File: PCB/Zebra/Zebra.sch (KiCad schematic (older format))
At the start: 10 parts, among them J1 Conn_01x05, J2 Conn_01x04, SW1 SW_Push, SW2 SW_Push, SW3 SW_Push, SW4 SW_Push

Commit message: Switch to foostan's footprint library, MIT license
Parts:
- SW1, SW2, SW3, SW4: footprint keyswitches:Kailh_socket_MX_optional -> kbd:CherryMX_Hotswap
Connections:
- net at SW1.1: now also J1.1 (Pin_1), SW2.1, SW3.1, SW4.1; no longer D1.2 (A)
- net at D2.2 (A): now also SW2.2; no longer SW2.1
- net at D3.2 (A): now also SW3.2; no longer SW3.1
- net at D4.2 (A): now also SW4.2; no longer SW4.1
- new net: D1.2 (A), SW1.2
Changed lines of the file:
@@
 Comment4 ""
 $EndDescr
-$Comp
-L Switch:SW_Push SW1
-U 1 1 5FA76D91
-P 2650 2000
-F 0 "SW1" H 2650 2285 50  0000 C CNN
-F 1 "SW_Push" H 2650 2194 50  0000 C CNN
-F 2 "keyswitches:Kailh_socket_MX_optional" H 2650 2200 50  0001 C CNN
-F 3 "~" H 2650 2200 50  0001 C CNN
-	1    2650 2000
-	1    0    0    -1
-$EndComp
 Wire Wire Line
 	2450 2000 2350 2000
@@
 F 0 "SW2" H 2650 2685 50  0000 C CNN
 F 1 "SW_Push" H 2650 2594 50  0000 C CNN
-F 2 "keyswitches:Kailh_socket_MX_optional" H 2650 2600 50  0001 C CNN
+F 2 "kbd:CherryMX_Hotswap" H 2650 2600 50  0001 C CNN
 F 3 "~" H 2650 2600 50  0001 C CNN
 	1    2650 2400
-	1    0    0    -1
+	-1   0    0    -1
 $EndComp
 $Comp
@@
 F 0 "SW3" H 2650 2985 50  0000 C CNN
 F 1 "SW_Push" H 2650 2894 50  0000 C CNN
-F 2 "keyswitches:Kailh_socket_MX_optional" H 2650 2900 50  0001 C CNN
+F 2 "kbd:CherryMX_Hotswap" H 2650 2900 50  0001 C CNN
 F 3 "~" H 2650 2900 50  0001 C CNN
 	1    2650 2700
-	1    0    0    -1
+	-1   0    0    -1
 $EndComp
 $Comp
@@
 F 0 "SW4" H 2650 3385 50  0000 C CNN
 F 1 "SW_Push" H 2650 3294 50  0000 C CNN
-F 2 "keyswitches:Kailh_socket_MX_optional" H 2650 3300 50  0001 C CNN
+F 2 "kbd:CherryMX_Hotswap" H 2650 3300 50  0001 C CNN
 F 3 "~" H 2650 3300 50  0001 C CNN
 	1    2650 3100
-	1    0    0    -1
+	-1   0    0    -1
 $EndComp
 $Comp
@@
 Wire Wire Line
 	1750 1600 1750 3100
+$Comp
+L Switch:SW_Push SW1
+U 1 1 5FA76D91
+P 2650 2000
+F 0 "SW1" H 2650 2285 50  0000 C CNN
+F 1 "SW_Push" H 2650 2194 50  0000 C CNN
+F 2 "kbd:CherryMX_Hotswap" H 2650 2200 50  0001 C CNN
+F 3 "~" H 2650 2200 50  0001 C CNN
+	1    2650 2000
+	-1   0    0    -1
+$EndComp
 $EndSCHEMATC

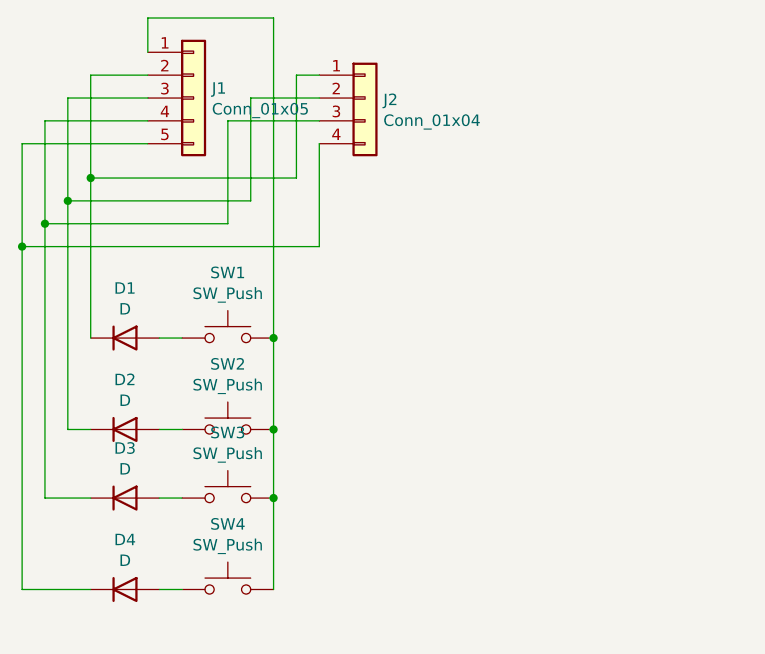
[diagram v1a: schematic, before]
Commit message: Add encoders
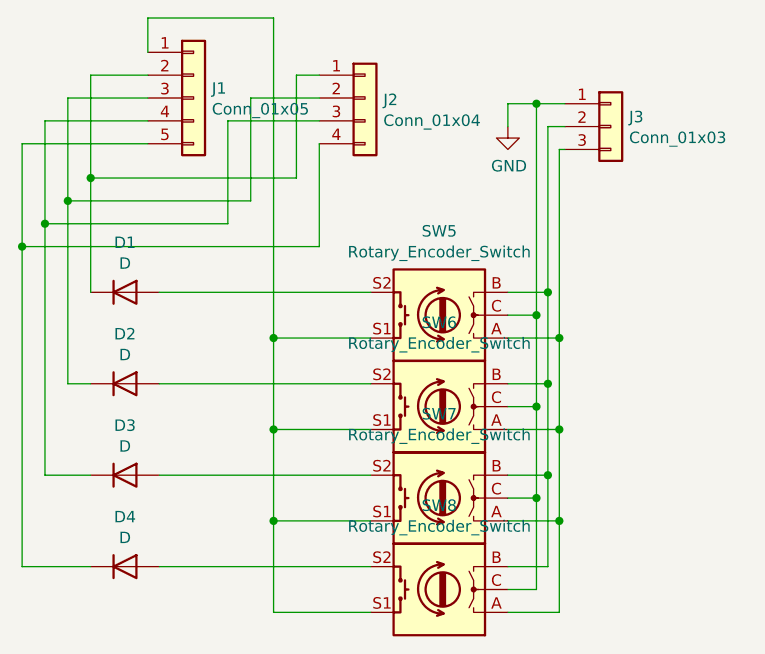
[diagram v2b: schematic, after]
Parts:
- removed SW1, SW2, SW3, SW4: SW_Push, kbd:CherryMX_Hotswap, symbol Switch:SW_Push
- added J3: Conn_01x03, Connector_PinHeader_2.54mm:PinHeader_1x03_P2.54mm_Vertical, symbol Connector_Generic:Conn_01x03
- added SW5, SW6, SW7, SW8: Rotary_Encoder_Switch, nk:CherryMX_Hotswap_Encoder, symbol Device:Rotary_Encoder_Switch
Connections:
- net at J1.1 (Pin_1): now also SW5.S1, SW6.S1, SW7.S1, SW8.S1
- net at D1.2 (A): now also SW5.S2
- net at D2.2 (A): now also SW6.S2
- net at D3.2 (A): now also SW7.S2
- net at D4.2 (A): now also SW8.S2
- new net: J3.2 (Pin_2), SW5.B, SW6.B, SW7.B, SW8.B
- new net: J3.3 (Pin_3), SW5.A, SW6.A, SW7.A, SW8.A
- new net GND: J3.1 (Pin_1), SW5.C, SW6.C, SW7.C, SW8.C
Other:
- moved on the sheet: D1, D2, D3, D4

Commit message: Rename switches, renumber
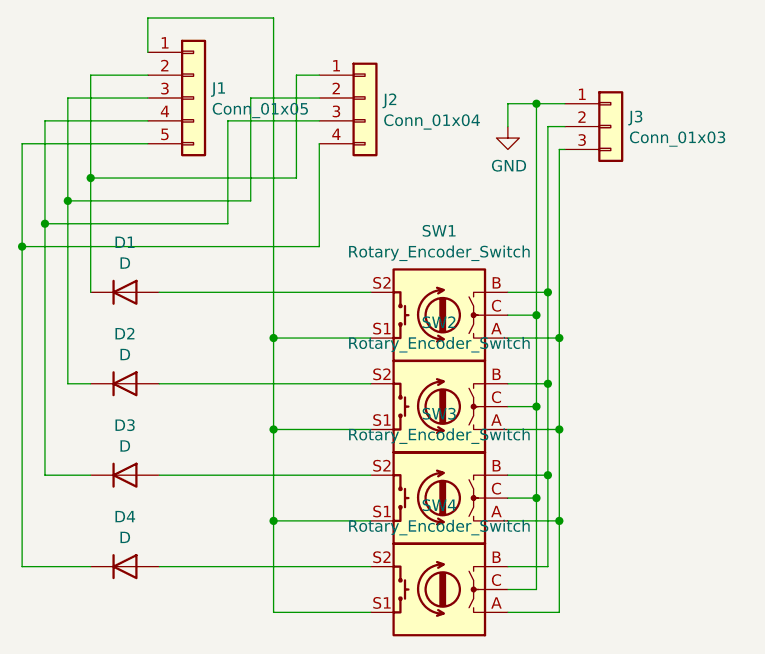
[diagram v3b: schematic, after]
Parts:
- renumbered SW5 to SW1, SW6 to SW2, SW7 to SW3, SW8 to SW4
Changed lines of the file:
@@
 $EndComp
 $Comp
-L Device:Rotary_Encoder_Switch SW5
+L Device:Rotary_Encoder_Switch SW1
 U 1 1 5FD10E8D
 P 3575 1900
-F 0 "SW5" H 3575 1533 50  0000 C CNN
+F 0 "SW1" H 3575 1533 50  0000 C CNN
 F 1 "Rotary_Encoder_Switch" H 3575 1624 50  0000 C CNN
 F 2 "nk:CherryMX_Hotswap_Encoder" H 3425 2060 50  0001 C CNN
@@
 	4100 1175 4100 2000
 $Comp
-L Device:Rotary_Encoder_Switch SW6
+L Device:Rotary_Encoder_Switch SW2
 U 1 1 5FD1A1FF
 P 3575 2300
-F 0 "SW6" H 3575 1933 50  0000 C CNN
+F 0 "SW2" H 3575 1933 50  0000 C CNN
 F 1 "Rotary_Encoder_Switch" H 3575 2024 50  0000 C CNN
 F 2 "nk:CherryMX_Hotswap_Encoder" H 3425 2460 50  0001 C CNN
@@
 	3275 2400 2850 2400
 $Comp
-L Device:Rotary_Encoder_Switch SW7
+L Device:Rotary_Encoder_Switch SW3
 U 1 1 5FD1CB31
 P 3575 2700
-F 0 "SW7" H 3575 2333 50  0000 C CNN
+F 0 "SW3" H 3575 2333 50  0000 C CNN
 F 1 "Rotary_Encoder_Switch" H 3575 2424 50  0000 C CNN
 F 2 "nk:CherryMX_Hotswap_Encoder" H 3425 2860 50  0001 C CNN
@@
 	3275 2800 2850 2800
 $Comp
-L Device:Rotary_Encoder_Switch SW8
+L Device:Rotary_Encoder_Switch SW4
 U 1 1 5FD24E4C
 P 3575 3100
-F 0 "SW8" H 3575 2733 50  0000 C CNN
+F 0 "SW4" H 3575 2733 50  0000 C CNN
 F 1 "Rotary_Encoder_Switch" H 3575 2824 50  0000 C CNN
 F 2 "nk:CherryMX_Hotswap_Encoder" H 3425 3260 50  0001 C CNN
@@
 Connection ~ 4100 2800
 $Comp
-L power:GND #PWR0101
+L power:GND #PWR01
 U 1 1 5FD3AC9C
 P 3875 1075
-F 0 "#PWR0101" H 3875 825 50  0001 C CNN
+F 0 "#PWR01" H 3875 825 50  0001 C CNN
 F 1 "GND" H 3880 902 50  0000 C CNN
 F 2 "" H 3875 1075 50  0001 C CNN
